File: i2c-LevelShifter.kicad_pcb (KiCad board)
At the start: 2 copper layers, 26.7 x 14.6 mm, 8 parts, among them P101 3v3, P102 5v, Q101 IRLML2502, Q102 IRLML2502

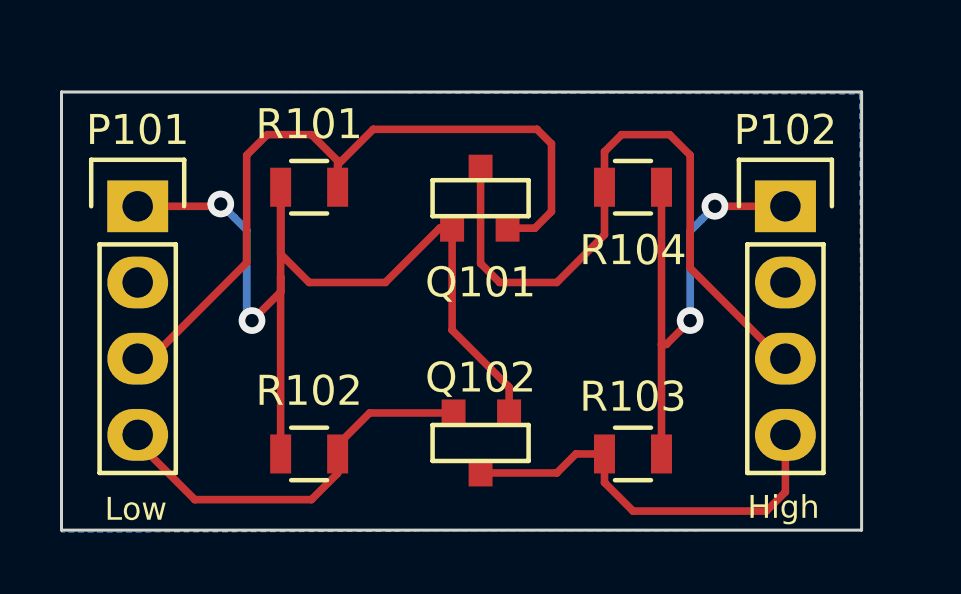
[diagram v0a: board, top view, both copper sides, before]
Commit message: New board layout and kiCad logo
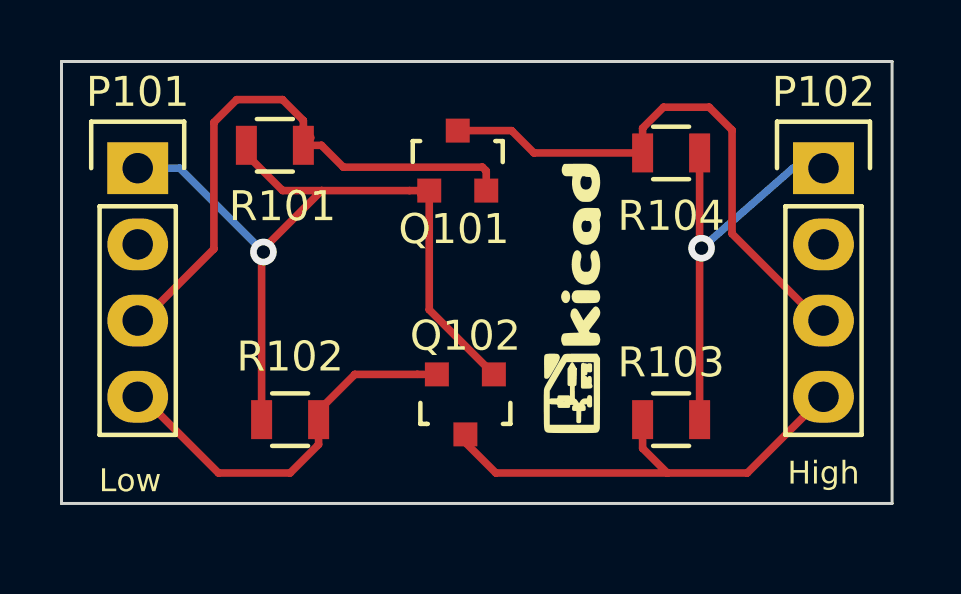
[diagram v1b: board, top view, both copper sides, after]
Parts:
- added G***: LOGO, i2cLib:kicad_logo, F.Cu at (164.3, 111.0)
- added G***: LOGO, i2cLib:kicad_logo_20mm, B.Cu at (161.3, 113.8)
- Q101, Q102: footprint i2cLib:Micro3 -> Housings_SOT-23_SOT-143_TSOT-6:SOT-23
- moved Q102 2.34 mm to (160.8, 114.6)
- moved R101 1.81 mm to (154.4, 105.9)
- moved P102 1.80 mm to (172.7, 106.7)
- moved R103 1.71 mm to (167.6, 115.1)
- moved R104 1.71 mm to (167.6, 106.2)
- moved R102 1.31 mm to (154.9, 115.1)
- moved P101 1.27 mm to (149.9, 106.7)
- moved Q101 0.80 mm to (160.5, 106.4)
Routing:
- net /VDD1=3v3: track 33.9 -> 28.2 mm, vias 2 -> 1
- net /SDA1: track 25.6 -> 20.1 mm
- net /SDA2: track 22.6 -> 18.6 mm
- net /VSS2=5v: track 16.7 -> 14.2 mm, vias 2 -> 1
- net /SCL2: track 13.9 -> 15.8 mm
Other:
- board size 26.7 x 14.6 mm -> 27.7 x 14.7 mm

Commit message: Corrected layout for P102 board edge
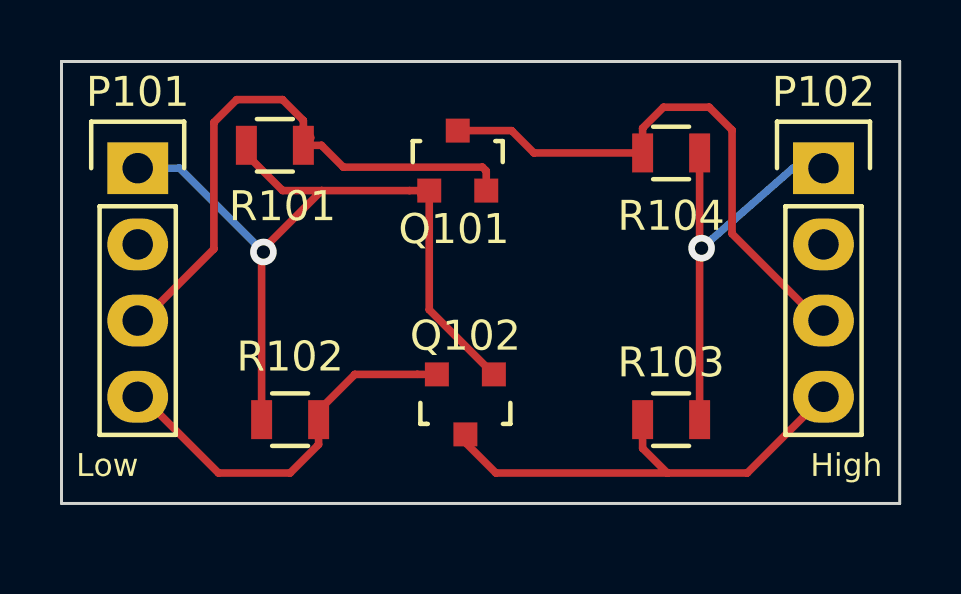
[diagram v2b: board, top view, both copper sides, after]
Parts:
- removed the G*** at (161.3, 113.8)
- G***: moved to B.Cu
- moved G*** 5.62 mm to (166.1, 116.3), turned to 180 degrees
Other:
- board size 27.7 x 14.7 mm -> 27.9 x 14.7 mm

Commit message: Changed the layout footprint to more suitable for Bread board
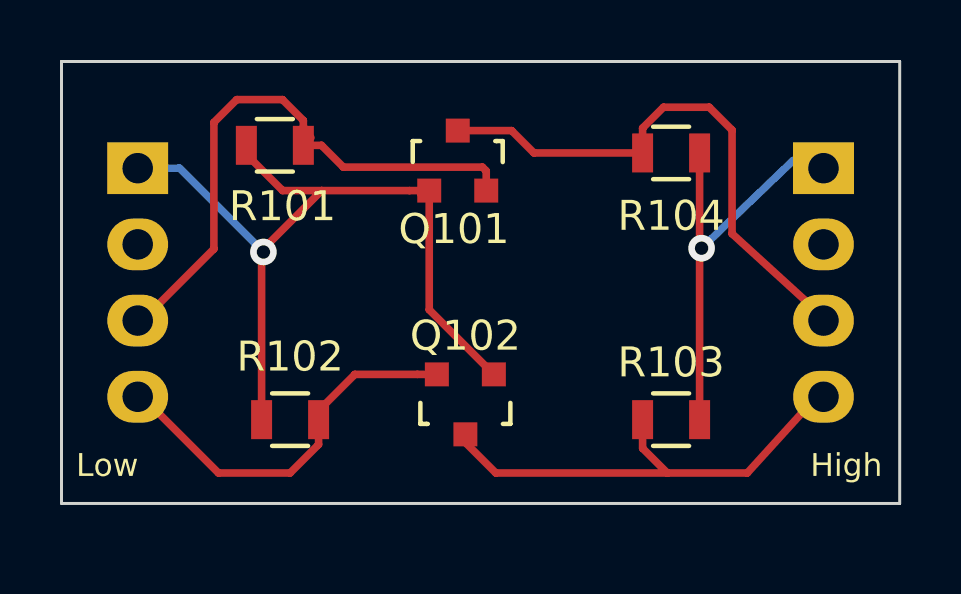
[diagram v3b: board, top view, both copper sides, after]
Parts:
- P101, P102: footprint Socket_Strips:Socket_Strip_Straight_1x04 -> Pin_Headers:Pin_Header_Straight_1x04; moved to B.Cu
- turned P101 to 180 degrees
- turned P102 to 180 degrees
